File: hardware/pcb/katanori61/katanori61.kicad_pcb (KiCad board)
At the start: 2 copper layers, 82 x 37.4 mm, 59 parts, among them J1 XIAO RISER, J10 BAT (JST-PH), J13 USB-C, J2 OLED, J4 SPK IN, J5 SPK OUT, J6 BTN2, J7 REED+TOGGLE, K31 G6S-2F DC5, Q1 MMUN2133LT1G, Q2 AO3401A, Q31 SS8050, U1 TPS61090RSAR, U2 MCP73871-2CCI/ML, U3 INA226AIDGSR, U4 AS5600-ASOM

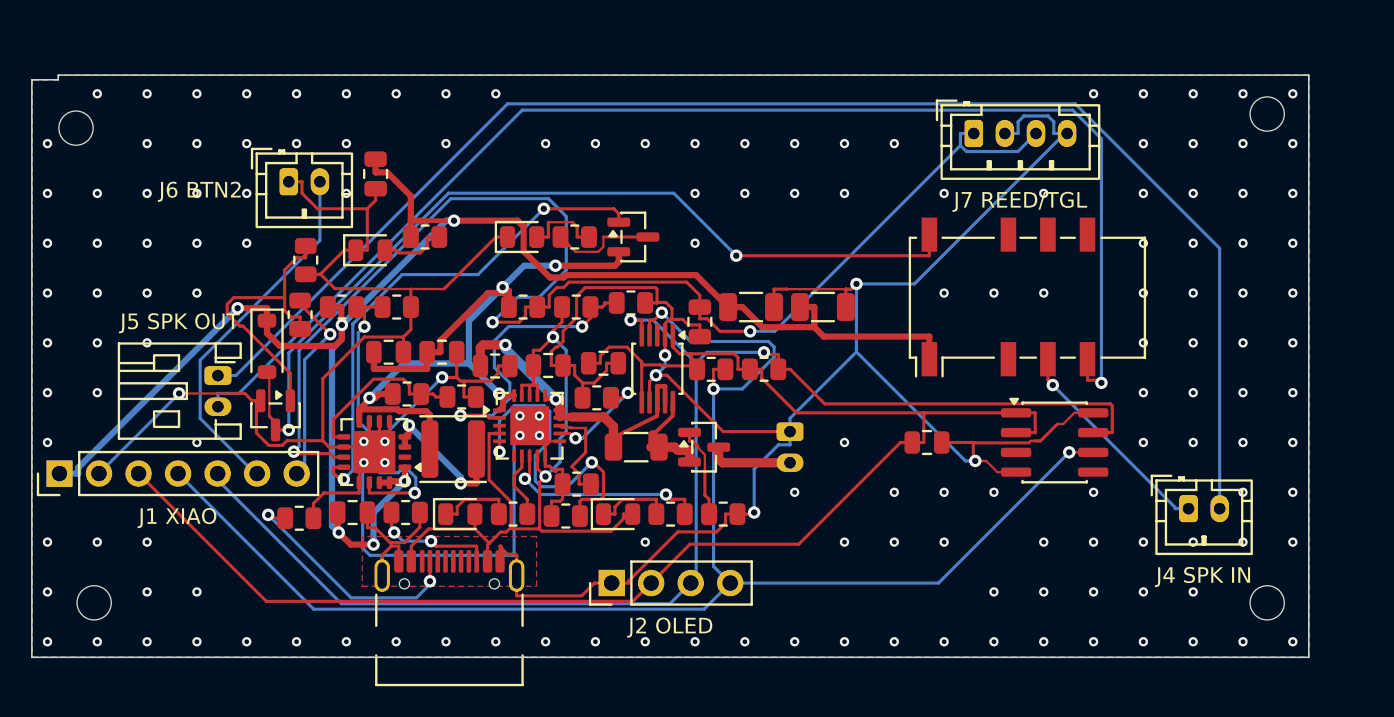
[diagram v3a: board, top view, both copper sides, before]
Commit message: pcb v6.1: 4 層にする／電池の口と USB-C を筐体に入る場所へ戻す
■ 口の位置（どちらも私が置き間違えていた）

J10（電池・JST-PH 縦・板の裏）を 板 X 46.59 → **73.5〜79.0**（電池の外）へ。
  電池は板の座標 X 16.05〜66.05 を占め、その上は板の裏まで 12.0 − 6.0 = 6.0 しか
  無い。縦の PH は挿して 8.0 要る（📄 ePH.pdf 1 ページ）。真ん中に置いて
  「6.0 に 8.0 が入るか」を測りに行っていたが、入る場所へ動かせば済む話だった。

J13（USB-C）を 前の縁 → **後ろの縁（ハッチ側）** へ。
  🔒 ユーザーの条件は「壁であればどこでもいい。ハッチ側でもいい」。前の縁は壁ではなく
  ReSpeaker の板（Z 8.2〜42.2）が立っていて、板の縁から背面まで 3.465・胴を 1.53 出すと
  残り 1.935 でプラグが入らない。条件の「壁であれば」を落として置いていた。

■ BACK_BANDS を消した（v61_board.py）

中身は「電池の上でない所」だったが、`BACK_BANDS`（裏の帯）という名前が実体を作り、
電池の厚みという一次の事実の代わりに引用できてしまった。🔒 ユーザー「BACK_BANDS は
貴方がた AI が作ったものであり、常に私から見れば死んでいる」。

  ⇒ BAT_BOX（電池の足跡）・BAT_T（6.0）・BOARD_UNDER_Z（12.0）だけを持ち、
    back_clear(x0,y0,x1,y1) がその場で引き算する。v61_map.py の検査も
    「帯の中か」から「下に何 mm 空いているか」に変えた。

■ 4 層（🔒 ユーザー 2026-09-17「4 層で行きましょう」）

2 層では U2（QFN-20・4×4）の 20 ピンが出入りできず、部品を動かすたびに別のネットが
切れていた（L1 の枠と U2 の枠の間が 0.4mm）。JLCPCB の見積もり 82×38・5 枚:
**2 層 $4.00 → 4 層 $7.00**（差 $3.00・1 枚 60 円）。

  F.Cu / In1.Cu（GND のベタ）/ In2.Cu / B.Cu。積層 1.6mm（プリプレグ 0.1 ＋
  コア 1.24 ＋ プリプレグ 0.1）。自動配線には F.Cu / In2.Cu / B.Cu の 3 層を見せる
  （内層を DSN の plane にすると Freerouting が落ちる・docs/VOICE-BOARD.md 10 章）。
  貫通穴は 2 層のときと同じ 0.6/0.3。統合基板の 0.45/0.2 はこの板の規則
  （穴 0.3 以上・環 0.13 以上）に掛かり、DRC が 69 件ずつ出た。

  ⚠ GND は 4 層でも自動配線に渡したまま。外してみたら U3（TSSOP-10）の 2 番と 7 番へ
    表のベタが届かず島が 4 つ残った（2 層のときと同じ症状）。

■ 途中で見つけて直したもの

- fab.py がガーバーの層名を書き写していて、**内層が出ないまま zip ができていた**。
  板の .kicad_pcb から読むようにした（board_copper()）。
- ケルビンと EP のビアを protect で渡すとき、穴の名前が 2 層の `Via[0-1]_800:400_um`
  のままだった。DSN に定義の無い穴を指すので Freerouting が**空の SES を黙って返す**。
  層数と穴径から名前を作るようにした。
- L1 の向きが逆で、SW のパッドが U1 と反対を向いていた（スイッチングノードが L1 を
  回り込む）。180° 回した。

■ 検算

未接続 0 ／ 回路図との差 0 ／ DRC エラー 0 ／ 銅のすきま 下回り 0。
配線 F.Cu 456・In2.Cu 193・B.Cu 52。ガーバーは In1_Cu / In2_Cu を含む銅 5 枚。
模型（v61_parts.scad 56 個）・STL・BOM・CPL も出し直した。

残る警告: lib_footprint_mismatch 4（留め穴・既知）／silk_edge_clearance 2（USB-C が
縁に載る）／silk_over_copper 2（1 番ピンの印の三角）／hole_to_hole 1（SCL と SDA のビア）。
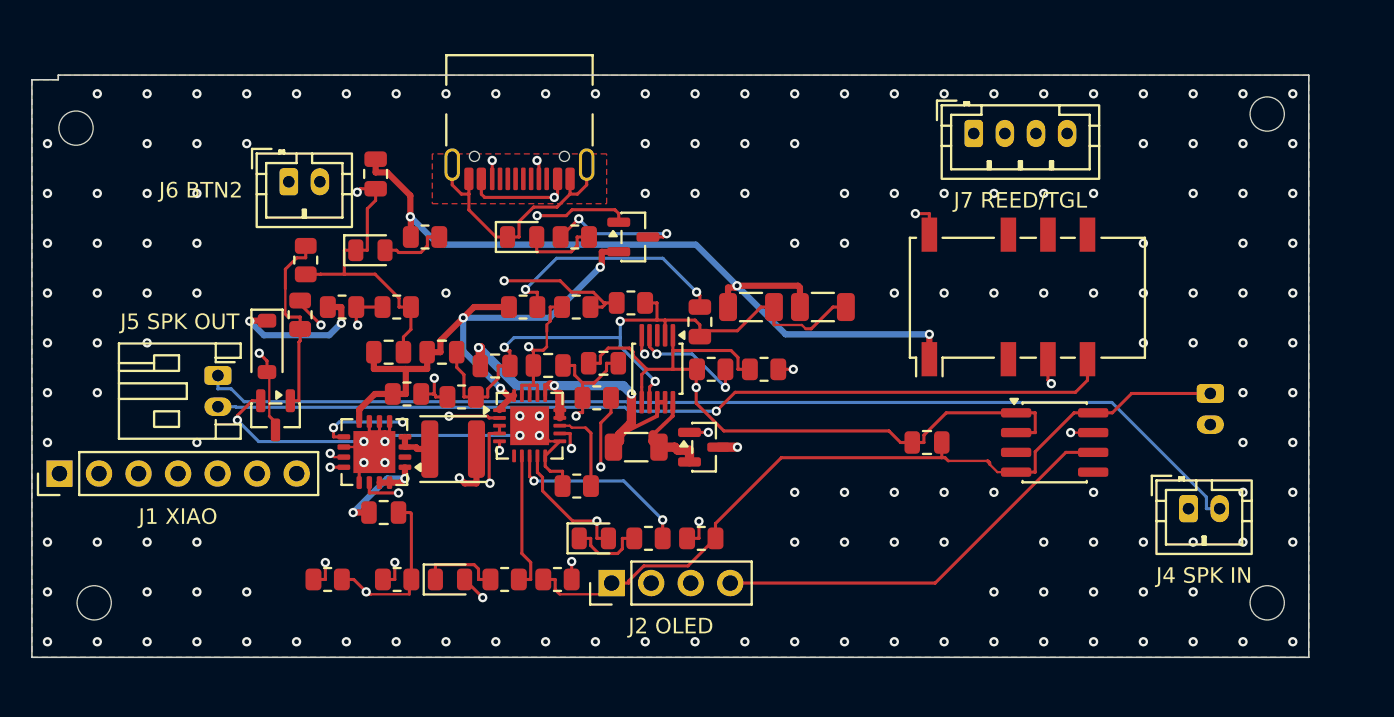
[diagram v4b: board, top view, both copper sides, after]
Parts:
- moved J13 33.0 mm to (71.3, 42.6), turned to 180 degrees
- moved J10 27.1 mm to (115.7, 60.5)
- moved R44 4.34 mm to (59.0, 72.4)
- moved R45 4.33 mm to (63.5, 72.4)
- moved LED3 4.25 mm to (66.9, 72.4)
- moved R14 4.23 mm to (70.4, 72.4)
- moved R15 4.11 mm to (73.8, 72.4)
- moved LED4 2.21 mm to (76.1, 69.8)
- moved R8 2.11 mm to (79.6, 69.8)
- moved R46 2.10 mm to (83.0, 69.8)
- moved C2 2.00 mm to (62.6, 68.1)
- moved R16 0.12 mm to (75.0, 66.4)
- turned L1 to 180 degrees
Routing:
- net BATRAW: track 5.44 -> 35.0 mm, vias 0 -> 1
- net SPKO: track 83.9 -> 58.2 mm
- net CC2: track 7.99 -> 33.7 mm
- net CC1: track 15.6 -> 41.1 mm
- net SPKM: track 92.1 -> 68.8 mm
- net VBUS: track 51.1 -> 68.5 mm, vias 2 -> 5
- net EN: track 87.4 -> 71.8 mm
- net LBO: track 32.9 -> 46.2 mm
- net COL: track 58.2 -> 70.7 mm
- net THERM: track 20.9 -> 10.8 mm
- net SDA: track 97.0 -> 88.0 mm, vias 3 -> 2
- net SW: track 9.81 -> 2.36 mm, vias 2 -> 0
- net BASE: track 18.8 -> 12.3 mm
- net STAT2: track 4.30 -> 8.94 mm
- net GND: track 280.5 -> 284.4 mm, vias 159 -> 163
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- added copper zone on In1.Cu, net GND
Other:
- copper layers 2 -> 4

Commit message: v6.1: 部品を格子に揃える／USB-C をハッチの中央へ／筐体を基板に追いつかせる
■ 基板

部品を揃えた（🔒 ユーザー「あまりにもガタガタで見苦しい」）。
  小さい部品は X 3.0 間隔、Y は 5.0 / 9.5 / 11.0 / 14.0 / 19.0 / 23.0 / 27.0 の列。
  主の道（J10 → Q2 → R41 → U2 → L1 → U1）は Y 14.0 の一直線。U2 だけ 15.5 で、
  下の辺 6〜10 番の逃げる帯を空けてある。U3 は R41 と同じ X 39.5。
  揃えたことで silk_over_copper 2 件が消えた。

USB-C を板の X 中央へ（枠 35.692〜46.332・中心 41.012 ＝ 板幅 82.024 の半分）。
出る長さを **引き算で出す**ようにした。1.53 は筐体の usbc_out() が **右の壁**から
引いた値で、口を後ろの縁へ移したのに値がそのままだった（奥まりが 0.8 のはずが
0.57 になっていた。たまたま浅い側だったので通っていただけ）。
  v61_board.usbc_out() = PCB_HATCH_GAP(0.5) + HATCH_T − USBC_RECESS(0.8)
  ⇒ ナイロン 1.3 / レジン 2.5。材料を変えれば追従する。

先に引く線を**座標の書き写しからやめた**。
  kelvin_tracks() … R41 と U3 のパッドから作る。書き写すと R41 か U3 を動かしたとき
    線がパッドから外れ、しかも **DRC は未接続を出さない**（別経路で繋がるため）ので
    黙って 10 倍に戻る。
  escape_stub()   … QFN の細ピッチのパッドから部品の外へ出す短い線。U2 の 9 番
    （VBUS）と 13 番（PROG1）に使う。廊下が 0.25mm しかなく、自動配線が通せずに
    そのピンだけ浮かせていた。

■ 筐体

USB-C の口を 右の壁 → **ハッチ（後ろ）** へ。5 か所:
  usbc_out()        右の壁からの式 → (IN_Y + HATCH_T − 0.8) − PCB_Y1
  USBC_X（新）      板の X 中央 43.012。USBC_Y は口の位置に使わなくなった
  usbc61()          模型を後ろの縁の中央へ（幅 8.94 が X・奥行 7.30 が Y）
  USBC_PORT_C/_SZ   ハッチの厚みの中央・[X, Z]
  usbc61_port_cut() port_cut(..., HATCH_T, "y")。p_rwall から p_hatch へ移した
  pcb_slide()       右の壁の USB-C が板を左へ押していた 1.2 → 0（もう押さない）

AS5600 を筐体側で描くのをやめた。基板の模型（PCB_PARTS の "U4"）が同じ 1 個を
持っていて、2 か所に描くと当たり検査が自分自身に当たっていた（pair_hub_knob が
15.791mm³）。模型が 9 個だった頃はこの二重描きが見えなかった。
磁石の高さも実寸から引き直し: MAG61_Z0 = AS_IC_Z + as_ic_h() + AS_GAP。
as_ic_h() は基板の模型から 1.75 を読む（筐体側は 1.1 と置いていた）。
  ⇒ 磁石の下面 15.8 → 16.45、つまみの軸 19.254 → 18.604。隙間 1.1 は設計値のまま。

■ 検算

基板: 未接続 0 ／ 回路図との差 0 ／ DRC エラー 0。
筐体: hit_hub 0 ／ hit_knob 0 ／ sk_hub 0 ／ sk_bat 0（どれも交わりが空）。
USB-C の奥まりはハッチの外面から 0.8（右の壁・XIAO と同じ関係）。
ハッチの足のねじ（X 43.749・Z 0.6〜2.4）とは Z が 11mm 離れている。

残る警告: lib_footprint_mismatch 4（留め穴・既知）／silk_edge_clearance 2（USB-C が
縁に載る）／hole_to_hole 2／track_dangling 1（自動配線が残した 0.19mm の切れ端）。
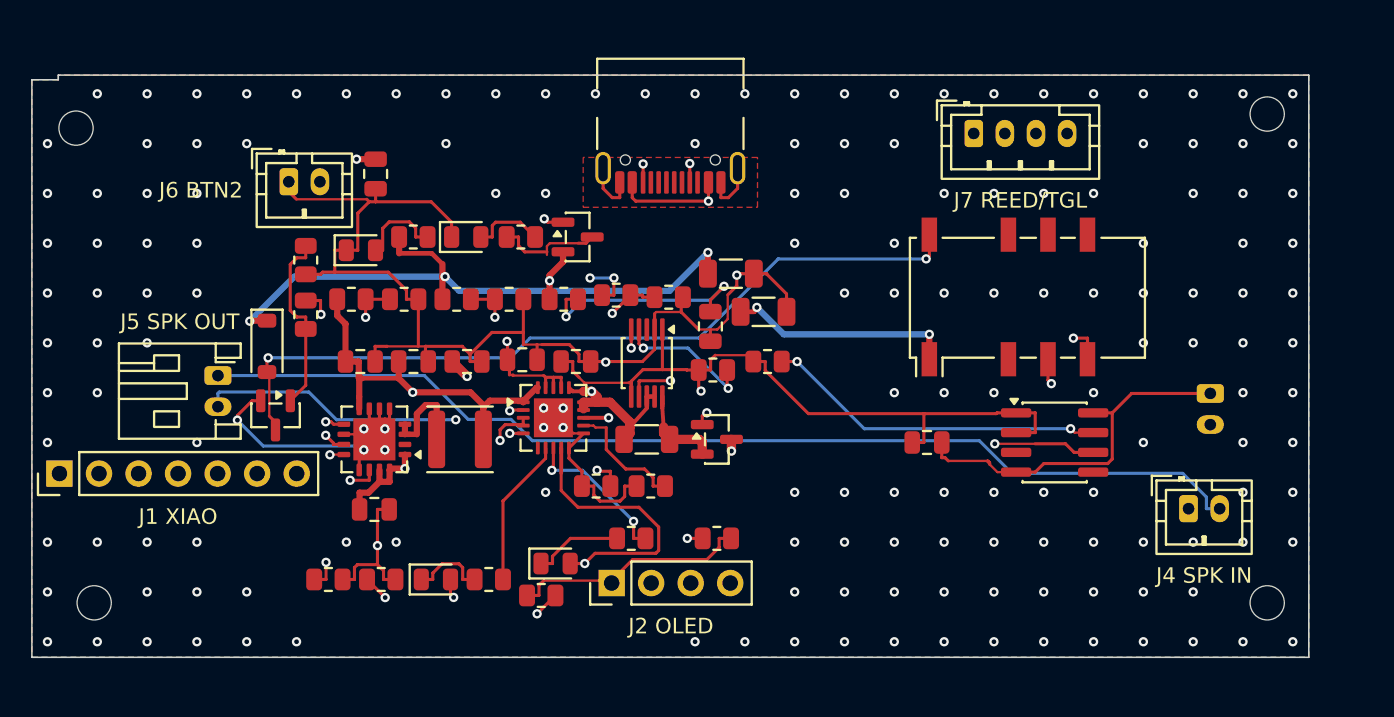
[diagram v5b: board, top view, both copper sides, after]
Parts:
- removed the LED2 at (61.7, 51.2)
- removed the R1 at (64.1, 60.5)
- removed the R2 at (67.6, 60.7)
- removed the R5 at (65.3, 50.4)
- removed the U3 at (80.2, 58.9)
- added Q1: MMUN2133LT1G, Package_TO_SOT_SMD:SOT-23, F.Cu at (75.1, 50.4)
- added R20: 1K, Resistor_SMD:R_0805_2012Metric, F.Cu at (71.4, 50.4)
- added R42: 10K, Resistor_SMD:R_0805_2012Metric, F.Cu at (83.7, 58.9)
- added R43: 10K, Resistor_SMD:R_0805_2012Metric, F.Cu at (87.3, 58.4)
- added R44: 5.1k, Resistor_SMD:R_0805_2012Metric, F.Cu at (59.0, 72.4)
- LED1: renamed from Q1; value MMUN2133LT1G -> RED; footprint Package_TO_SOT_SMD:SOT-23 -> LED_SMD:LED_0805_2012Metric
- LED2: renamed from LED1; value RED -> WHITE
- R1: renamed from R42; value 10K -> 1.87M
- R2: renamed from R43; value 10K -> 330K
- U3: renamed from R44; value 5.1k -> INA226AIDGSR; footprint Resistor_SMD:R_0805_2012Metric -> Package_SO:TSSOP-10_3x3mm_P0.5mm
- moved U3 24.8 mm to (79.5, 58.5), turned to 270 degrees
- moved R2 23.6 mm to (63.9, 54.4)
- moved R1 23.5 mm to (60.5, 54.4)
- moved LED1 10.7 mm to (67.9, 50.4)
- moved LED2 10.4 mm to (61.1, 51.2)
- moved R5 10.4 mm to (64.5, 50.4)
- moved J13 9.69 mm to (81.0, 42.9)
- moved R3 7.38 mm to (67.3, 54.4)
- moved R4 7.24 mm to (70.7, 54.4)
- moved R17 6.65 mm to (79.8, 66.4)
- moved C9 3.82 mm to (87.0, 55.2)
- moved LED4 2.94 mm to (73.6, 71.4)
- moved R6 2.68 mm to (77.5, 54.1)
- moved R13 2.66 mm to (74.2, 54.4)
- moved C6 2.50 mm to (84.9, 52.8)
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- renumbered R20 to R5
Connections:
- LED1 pad 1: LBO -> GND
- LED1 pad 2: VSYS -> N_LED1
- LED2 pad 2: N_LED1 -> N_LED2
- R1 pad 1: V33 -> VSYS
- R1 pad 2: SDA -> LBI
- R2 pad 1: V33 -> LBI
- R2 pad 2: SCL -> GND
- R5 pad 1: N_Q1C -> V5
- R5 pad 2: N_LED1 -> N_LED2
- U3 pad 1: CC1 -> V33
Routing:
- net VBUS: track 68.5 -> 89.4 mm, vias 5 -> 7
- net LBO: track 46.2 -> 25.4 mm
- net COL: track 70.7 -> 51.5 mm
- net VSYS: track 52.1 -> 40.0 mm, vias 4 -> 2
- net FB: track 17.3 -> 28.2 mm
- net CC1: track 41.1 -> 50.8 mm
- net V5: track 106.6 -> 115.6 mm
- net CC2: track 33.7 -> 40.9 mm
- net SPKO: track 58.2 -> 65.0 mm, vias 1 -> 2
- net SCL: track 91.5 -> 84.8 mm
- net GND: track 284.4 -> 290.9 mm, vias 163 -> 168
- net BATG: track 9.03 -> 14.9 mm
- net SW: track 2.36 -> 6.44 mm
- net THERM: track 10.8 -> 14.9 mm
- net VLIPO: track 23.8 -> 20.3 mm, vias 3 -> 2
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
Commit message: v6.1: USB-C の出を 2.5 に／ナイロンは板を 0.4 前へ（箱は変えない）
🔒 ユーザー 2026-09-17「2.5 で。その上でナイロン版は基板を 0.4 手前にずらして」。

■ 出る量を 2.5 に（深いほう＝レジンに合わせる）

板の銅は出る量を 1 つしか持てない。レジン（ハッチ 2.8）が要求する 2.5 に合わせた。
  usbc_out() = PCB_HATCH_GAP + HATCH_T_RESIN − USBC_RECESS ＝ 2.5
⚠ 「2.6 を超えると前のシェルの足が板から外れる」という上限は、足形が **NoFrontLegs**
  （前の足が無い）になった時点で当たらない。実際の上限は一番縁寄りのパッドが板から
  出ないことで、いま板 Y 34.170・縁 37.4 まで 3.23 余っている。

⭐ 枠ではなく **胴** で位置を決めるようにした（org_from_box の key="Fab"・BOX_BY_FAB）。
  枠（courtyard）は KiCad が付けた逃げで、USB-C では胴より後ろへ 0.5 大きい。枠に
  2.5 を当てると胴は 2.0 しか出ない。直前のコミットでここを取り違えて、奥まりを
  0.8 にするつもりが 1.3 にしていた（別セッションの指摘で気づいた）。

■ ナイロンは板を 0.4 前へ。箱は変えない

  PCB_Y0 = nylon() ? 13.1 : 13.5   （PCB_Y1 = PCB_Y0 + 37.4）
  PCB_HATCH_GAP = nylon() ? 0.9 : 0.5
この 2 つが対で効き、IN_Y はどちらの材料でも 51.4 のまま ＝ **箱の外形は同じ**。
  ナイロン: ハッチ外面 53.0 / 口の面 53.0 → 面一
  レジン  : ハッチ外面 54.2 / 口の面 53.4 → 奥まり 0.80（右の壁・XIAO と同じ関係）
⚠ 板を動かすだけでは差は変わらない。ハッチは板から測って作る（IN_Y = PCB_Y1 + 逃げ）ので、
  板を動かすとハッチも一緒に動く。**逃げと対で**動かして初めて板だけが寄る。

KNOB_AT を板に追従させた（+ (PCB_Y0 − 13.5)）。磁石は板の上の AS5600 を読むので、
板が前へ寄ればつまみも同じだけ寄らないとずれる（ナイロンで 0.4 ずれていた）。

■ 模型の置き方を板から引くようにした

pcb61_solid() が translate([−38.0, 90.9, …]) と直書きで、板を 13.5 → 13.1 に動かしたとき
模型だけ 0.4 後ろに残り、**USB-C がハッチから飛び出して見えた**（🔒 ユーザーが絵で発見）。
  translate([HUB_AT[0] − 40.0, PCB_Y0 + 40.0 + PCB_W, HUB_AT[2]])
数字は合っていたが絵が合っていなかった。見てもらわなければ気づいていない。

■ あわせて直した 2 件（別セッションの報告から）

・hole_to_hole 3 件 … 自動配線が銅の間隔ちょうど（0.15）までビアを寄せるが、規則は
  **穴どうし** 0.5 を見る。穴の間隔 ＝ 銅の間隔 ＋（銅径 0.6 − 穴径 0.3）なので、
  ビア同士だけ銅を 0.2 空ける（DSN に (clearance 2000 (type via_via))）。
・track_dangling 1 件 … 取り込みで浮いた切れ端を落とす掃除（route.py の prune_dangling）。

■ 検算

基板: 未接続 0 ／ 回路図との差 0 ／ DRC エラー 0 ／ 銅のすきま 下回り 0。
      残る警告は lib_footprint_mismatch 4 件（留め穴・既知）だけ。silk_edge_clearance も消えた。
筐体: hit_hub 0 ／ hit_knob 0 ／ sk_hub 0（体積 0）／ sk_bat 0（体積 0）。
      AS5600 と磁石のずれは両材料とも 0。
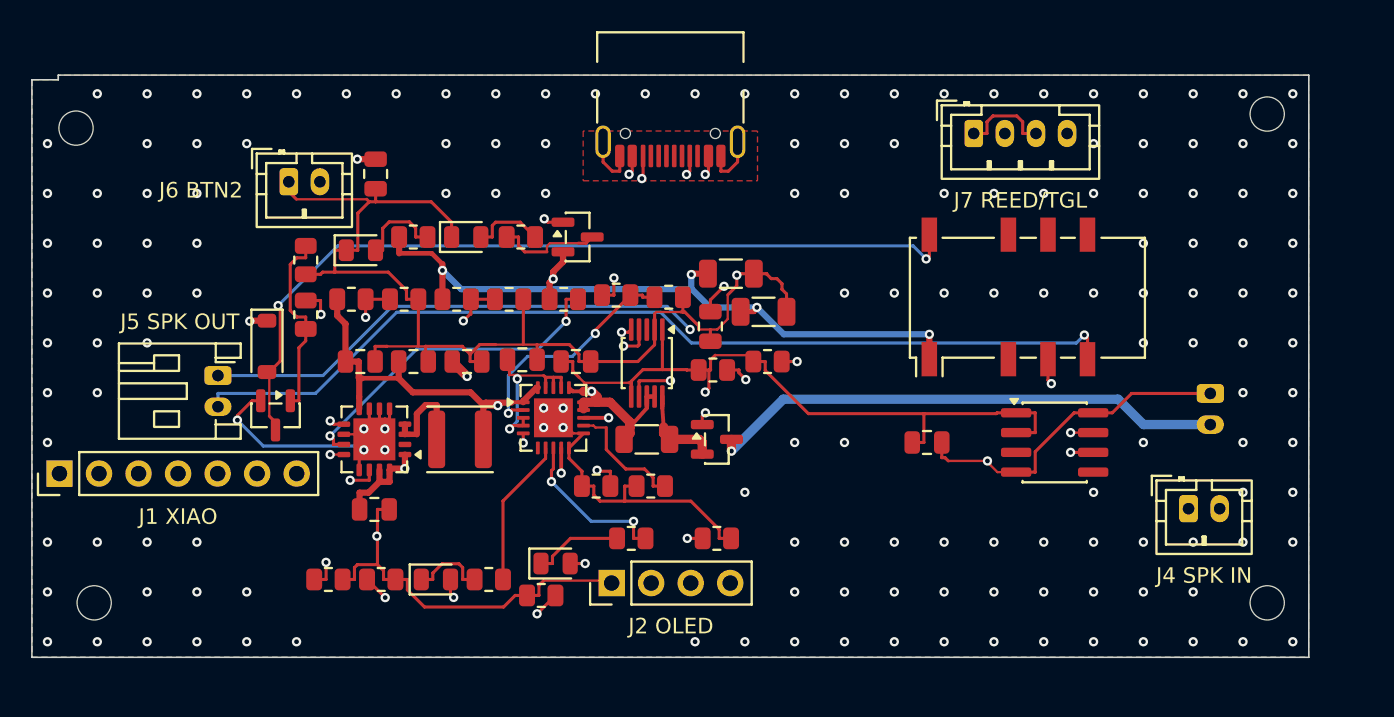
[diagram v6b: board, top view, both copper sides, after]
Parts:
- moved J13 1.70 mm to (81.0, 41.1)
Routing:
- net VBUS: track 89.4 -> 65.9 mm, vias 7 -> 8
- net LBO: track 25.4 -> 35.9 mm
- net SCL: track 84.8 -> 94.6 mm
- net EN: track 70.3 -> 60.7 mm
- net CC1: track 50.8 -> 42.8 mm
- net SPKM: track 68.3 -> 75.4 mm, vias 0 -> 1
- net V5: track 115.6 -> 109.1 mm
- net GND: track 290.9 -> 297.1 mm, vias 168 -> 160
- net VPCC: track 20.3 -> 15.2 mm
- net BATG: track 14.9 -> 10.4 mm
- net V33: track 102.1 -> 98.1 mm
- net CC2: track 40.9 -> 36.9 mm
- net SPKO: track 65.0 -> 61.3 mm, vias 2 -> 1
- net COL: track 51.5 -> 53.9 mm
- net SDA: track 87.4 -> 89.6 mm
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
